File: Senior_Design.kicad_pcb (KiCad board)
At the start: 2 copper layers, 100 x 100 mm, 149 parts, among them J101 BARREL_JACK, J102 touch(8pos) AT42QT1070 STANDA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, J103 ISP, J104 GS3, J105 GS3, J106 GS3, J107 LoadCell_Conn, J108 Smraza2004_LCD, J109 ambientLight, J110 GS3, J1101 BLE_RESET, J111 RESET, J112 Serial Monitor, J113 breakout, J114 GS2, J115 GS2, J301 GS2, J501 USB_A, J502 USB_A, Q1101 BSS138, Q1102 BSS138, Q301 MMBT4403, U1001 INA169, U102 WS2812B, U103 WS2812B_STRIP, U104 ATMEGA328PB-AU, U1101 LM358_IC, U1102 LP2985-3.3, U201 TPS562210, U301 HX711, U401 MOUDLE-BLUETOOTH-HC-05(34P-27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, U601 TPS562210, U901 INA169, Y101 16MHZ

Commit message: traces started
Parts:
- removed C101: 0.1uF, Capacitors_SMD:C_0603
- removed D202, D602: LED, LEDs:LED_0805
- removed J114, J115: GS2, Connectors:GS2
- removed R206, R606: 1K, Resistors_SMD:R_0603
- removed R401: 10K, Resistors_SMD:R_0603
- removed S401: button, Buttons_Switches_THT:SW_PUSH_6mm
- added C104: 0.1uF, Capacitors_SMD:C_0603, F.Cu at (105.0, 122.0)
- added D105: LED, LEDs:LED_0603, F.Cu at (111.0, 102.0)
- added D106: LED, LEDs:LED_0603, F.Cu at (111.0, 105.0)
- added D1105: LED, LEDs:LED_0603, F.Cu at (76.0, 67.0)
- added J1102: GS2, Connectors:GS2, F.Cu at (60.4, 110.0)
- added J1103: GS2, Connectors:GS2, F.Cu at (54.0, 110.0)
- added J117: GS3, Connectors:GS3, F.Cu at (126.0, 106.0)
- added J118: GS3, Connectors:GS3, F.Cu at (119.0, 106.0)
- added J119: ext_5VPWR, Pin_Headers:Pin_Header_Straight_1x04_Pitch2.54mm, F.Cu at (107.0, 113.0)
- added J123: GS2, Connectors:GS2, F.Cu at (91.2, 76.6)
- added J124: ext_Motion, Pin_Headers:Pin_Header_Straight_1x03_Pitch2.54mm, F.Cu at (101.0, 122.0)
- added J302: GS2, Connectors:GS2, F.Cu at (66.0, 118.0)
- added J401: GS2, Connectors:GS2, F.Cu at (137.0, 107.0)
- added J402: GS2, Connectors:GS2, F.Cu at (137.0, 128.0)
- added R109: 500, Resistors_SMD:R_0805_HandSoldering, F.Cu at (107.0, 102.0)
- added R110: 500, Resistors_SMD:R_0805_HandSoldering, F.Cu at (107.0, 105.0)
- added R1112: 500, Resistors_SMD:R_0805_HandSoldering, F.Cu at (71.0, 67.0)
- added R1113: 500, Resistors_SMD:R_0805_HandSoldering, F.Cu at (55.0, 64.0)
- added R801: 10, Resistors_THT:R_Axial_DIN0309_L9.0mm_D3.2mm_P5.08mm_Vertical, F.Cu at (122.0, 89.0)
- added R802: RL, Resistors_THT:R_Axial_DIN0309_L9.0mm_D3.2mm_P5.08mm_Vertical, F.Cu at (132.0, 85.0)
- added R902: 10, Resistors_THT:R_Axial_DIN0309_L9.0mm_D3.2mm_P5.08mm_Vertical, F.Cu at (137.0, 89.0)
- added R903: RL, Resistors_THT:R_Axial_DIN0309_L9.0mm_D3.2mm_P5.08mm_Vertical, F.Cu at (117.0, 85.0)
- C112, C113: value 22pF -> 20pF
- C204, C604: footprint Capacitors_SMD:C_0603 -> Capacitors_SMD:C_0402
- D101, D102, D103, D104, D1103, D401: footprint LEDs:LED_0805 -> LEDs:LED_0603
- D1104, D201, D501, D502, D601: footprint Diodes_SMD:D_SOD-123F -> sod:SOD-128
- L201, L601: footprint Inductors_SMD:L_Vishay_IHLP-1212 -> Inductors_SMD:L_Taiyo-Yuden_MD-5050
- R101, R107, R108, R301, R302: footprint Resistors_SMD:R_0603 -> Resistors_SMD:R_0805_HandSoldering
- R102: value 1K -> 500; footprint Resistors_SMD:R_0603 -> Resistors_SMD:R_0805_HandSoldering
- R103, R1102, R1104: value 330 -> 500; footprint Resistors_SMD:R_0603 -> Resistors_SMD:R_0805_HandSoldering
- R1101: value 1k -> 10k
- R1103: value 33K -> 54.9K
- R1105: value 220 -> 100; footprint Resistors_SMD:R_0603 -> Resistors_SMD:R_0805_HandSoldering
- R201, R601: value 10.0k -> 10k
- R203, R603: value 54.9k -> 59k
- R204, R604: value 10k -> 10k_FB
- R205, R605: value 0.1 -> 0.1_SHUNT; footprint Resistors_SMD:R_0603 -> Resistors_SMD:R_1206
- R406: value 2K -> 500; footprint Resistors_SMD:R_0603 -> Resistors_SMD:R_0805_HandSoldering
- RV1101: footprint Potentiometers:Potentiometer_Trimmer_ACP_CA9v_Horizontal_Px10.0mm_Py5.0mm -> SparkFun-Electromechanical:TSR-3386U
- U1001, U901: footprint sot:SOT23-5 -> TO_SOT_Packages_SMD:SOT-23-5
- U201, U601: value TPS562210 -> TPS563210ADDFT
- U301: footprint sop:SSOP16 -> soic:SOIC16
- moved D1103 22.5 mm to (113.0, 125.0), turned to 0 degrees
- moved R1104 21.6 mm to (113.0, 122.0), turned to 0 degrees
- moved C111 19.4 mm to (92.0, 82.0), turned to 180 degrees
- moved C110 19.1 mm to (92.0, 80.0), turned to 180 degrees
- moved D401 13.6 mm to (76.0, 70.0)
- moved R406 12.6 mm to (71.0, 70.0)
- moved D103 12.5 mm to (104.0, 68.0), turned to 180 degrees
- moved R405 12.5 mm to (64.0, 68.0), turned to 90 degrees
- moved R1101 9.22 mm to (105.0, 125.0), turned to 180 degrees
- moved R107 8.54 mm to (105.0, 65.0), turned to 180 degrees
- moved J102 8.25 mm to (90.0, 113.0)
- moved C303 7.62 mm to (67.0, 129.0), turned to 180 degrees
- moved J109 6.71 mm to (111.0, 76.0)
- moved D501 6.40 mm to (133.0, 107.0)
- moved D502 6.40 mm to (133.0, 128.0)
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- renumbered S101 to SW101, J111 to SW102, J1101 to SW1101
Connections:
- net BT_PWR renamed /Bluetooth/PwrOn
- C106 pad 2: 5V-BUS -> 5V-BUS_USBLINE
- C107 pad 2: 5V-BUS -> 5V-BUS_USBLINE
- C108 pad 2: 5V-BUS -> 5V-BUS_USBLINE
- C110 pad 2: 5V-BUS -> Net-(C110-Pad2)
- C111 pad 2: 5V-BUS -> Net-(C110-Pad2)
- C305 pad 2: 3V3-BUS -> 5V-BUS
- C306 pad 1: 3V3-BUS -> 5V-BUS
- D1104 pad 2: 3V3-BUS -> 5V-BUS
- D201 pad 1: 5V-BUS -> /_5V_SYS
- D501 pad 2: /USB/5V -> 5V-BUS_USBLINE
- D502 pad 2: /USB/5V -> 5V-BUS_USBLINE
- D601 pad 1: 5V-BUS_USBLINE -> /_5V_USB
- J103 pad 2: (no net) -> 5V-BUS
- Q301 pad 3: 3V3-BUS -> 5V-BUS
- R103 pad 1: (no net) -> LED_Din
- R107 pad 2: Net-(J114-Pad1) -> MCU_TX
- R108 pad 2: Net-(J115-Pad1) -> MCU_RX
- R1101 pad 2: (no net) -> Motion_Signal
- R1110 pad 2: 3V3-BUS -> 5V-BUS
- R1111 pad 2: 3V3-BUS -> 5V-BUS
- R305 pad 1: 3V3-BUS -> 5V-BUS
- U102 pad 1: 5V-BUS -> 5V-BUS_USBLINE
- U103 pad 3: 5V-BUS -> 5V-BUS_USBLINE
- U104 pad 18: 5V-BUS -> Net-(C110-Pad2)
- U104 pad 2: (no net) -> BT_KEY
- U104 pad 20: 5V-BUS -> Net-(C110-Pad2)
- U104 pad 23: (no net) -> Motion_Signal
- U104 pad 4: 5V-BUS -> Net-(C110-Pad2)
- U104 pad 9: LEDS_Din -> LED_Din
- U301 pad 1: 3V3-BUS -> 5V-BUS
- U301 pad 16: 3V3-BUS -> 5V-BUS
- U401 pad 1: B_RX -> /Bluetooth/TX_3v3
- U401 pad 11: Net-(R401-Pad2) -> (no net)
- U401 pad 2: B_TX -> /Bluetooth/RX_3v3
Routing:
- net 5V-BUS: track 0.00 -> 186.8 mm, vias 0 -> 6
- net 5V-BUS_USBLINE: track 0.00 -> 70.6 mm, vias 0 -> 2
- net +12V: track 99.3 -> 144.1 mm
- net /Bluetooth/3_3V: track 0.00 -> 31.9 mm, vias 0 -> 4
- net /5V-Regulator/PG: track 16.8 -> 48.3 mm, vias 2 -> 4
- net Net-(RV1101-Pad2): track 0.00 -> 31.3 mm
- net 5V_curMon+_USBLINE: track 0.00 -> 29.5 mm, vias 0 -> 2
- net Net-(D1102-Pad2): track 0.00 -> 25.8 mm
- net /Bluetooth/RX_3v3: track 2.15 -> 26.6 mm
- net /Bluetooth/TX_3v3: track 2.15 -> 25.5 mm
- net 5V_curMon+: track 15.1 -> 37.0 mm, vias 0 -> 2
- net Net-(R401-Pad2): track 20.0 -> 0.00 mm
- net /_5V_USB: track 0.00 -> 18.3 mm
- net Net-(J117-Pad3): track 0.00 -> 17.0 mm
- net Net-(C110-Pad2): track 0.00 -> 15.5 mm
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
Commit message: 99 percent ready to order
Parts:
- removed R801, R902: 10, Resistors_THT:R_Axial_DIN0309_L9.0mm_D3.2mm_P5.08mm_Vertical
- moved R704 26.0 mm to (127.2, 114.0), turned to 270 degrees
- moved R703 22.0 mm to (127.2, 111.0), turned to 270 degrees
- moved R702 21.7 mm to (121.0, 114.8), turned to 270 degrees
- moved R903 18.0 mm to (134.9, 84.0)
- moved R701 16.6 mm to (121.0, 112.0), turned to 270 degrees
- moved R802 15.5 mm to (116.5, 84.0)
- moved R901 15.2 mm to (119.8, 94.0)
- moved U901 15.2 mm to (120.8, 98.0)
- moved R1001 14.9 mm to (134.9, 94.0)
- moved U1001 14.8 mm to (135.8, 98.0)
- moved C104 6.75 mm to (98.3, 122.8), turned to 90 degrees
- moved C107 5.10 mm to (110.0, 53.0), turned to 90 degrees
- moved J106 4.08 mm to (108.8, 92.0)
- moved R102 3.43 mm to (138.4, 58.2)
- moved D101 3.37 mm to (134.4, 58.2)
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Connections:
- J501 pad 5: Net-(J501-Pad5) -> GND
- J502 pad 5: Net-(J502-Pad5) -> GND
- R202 pad 1: /5V-Regulator/PG -> 5V_curMon+
- R202 pad 2: 5V_curMon+ -> Net-(R202-Pad2)
- R602 pad 1: /5V-Regulator/PG -> 5V_curMon+_USBLINE
- R602 pad 2: 5V_curMon+_USBLINE -> Net-(R602-Pad2)
- U201 pad 4: /5V-Regulator/PG -> Net-(R202-Pad2)
- U601 pad 4: /5V-Regulator/PG -> Net-(R602-Pad2)
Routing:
- net 5V-BUS: track 186.8 -> 432.6 mm, vias 6 -> 13
- net GND: track 14.5 -> 183.0 mm, vias 7 -> 37
- net SDA: track 3.28 -> 90.4 mm, vias 0 -> 1
- net SCL: track 3.41 -> 88.4 mm, vias 0 -> 1
- net 5V-BUS_USBLINE: track 70.6 -> 148.4 mm, vias 2 -> 6
- net breakout_1A: track 0.00 -> 77.3 mm, vias 0 -> 1
- net BT_STATE: track 0.00 -> 70.6 mm, vias 0 -> 2
- net /Bluetooth/3_3V: track 31.9 -> 101.8 mm, vias 4 -> 6
- net LED_Din: track 0.00 -> 64.2 mm, vias 0 -> 2
- net MOSI: track 0.00 -> 63.2 mm, vias 0 -> 1
- net RESET: track 13.0 -> 75.5 mm, vias 0 -> 2
- net B_RX: track 11.8 -> 74.3 mm, vias 0 -> 1
- net breakout_2A: track 0.00 -> 62.4 mm, vias 0 -> 1
- net SCK: track 3.14 -> 61.8 mm, vias 0 -> 2
- net MISO: track 0.00 -> 57.6 mm, vias 0 -> 1
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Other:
- board text added: "5V D GND"
- board text added: "5V GND 5V_USB GND"
- board text added: "5V SIG GND"
- board text added: "Bluetooth"
- board text added: "Bluetooth RESET"
- board text added: "E+ E- A- A+"
- board text added: "EXTERNAL 5V POWER"
- board text added: "GND 5V SDA SCL"
- board text added: "GND LED 5V"
- board text added: "MCU RESET"
- board text added: "MISO-VCC SCK-MOSS RES-GND"
- board text added: "Monitor"
- board text added: "PC3 PE2 5V GND"
- board text added: "PE0 PE1 PB0 PB1"
- board text added: "RX TX"
- board text added: "UART"
- board text added: "UCF Senior Design Smart Table"

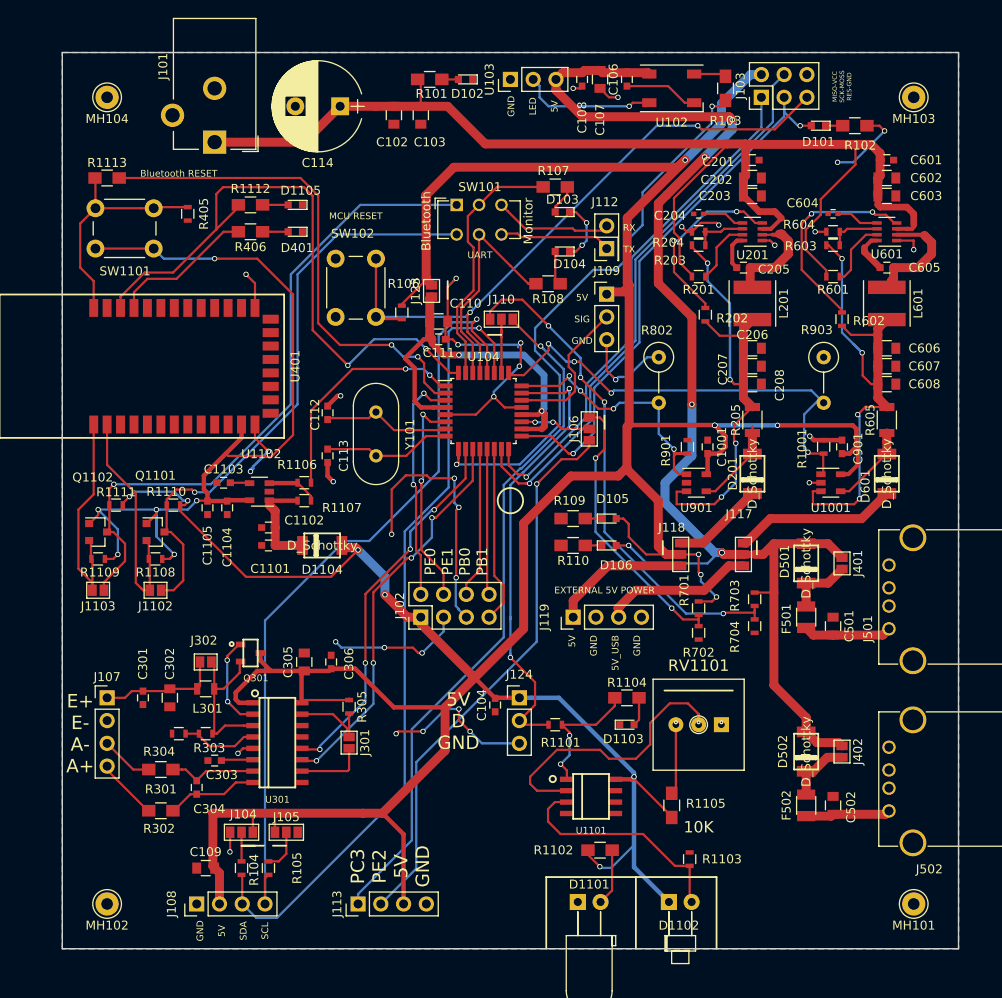
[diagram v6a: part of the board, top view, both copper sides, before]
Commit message: finalized pcblayouts, before uploading to manufacturer
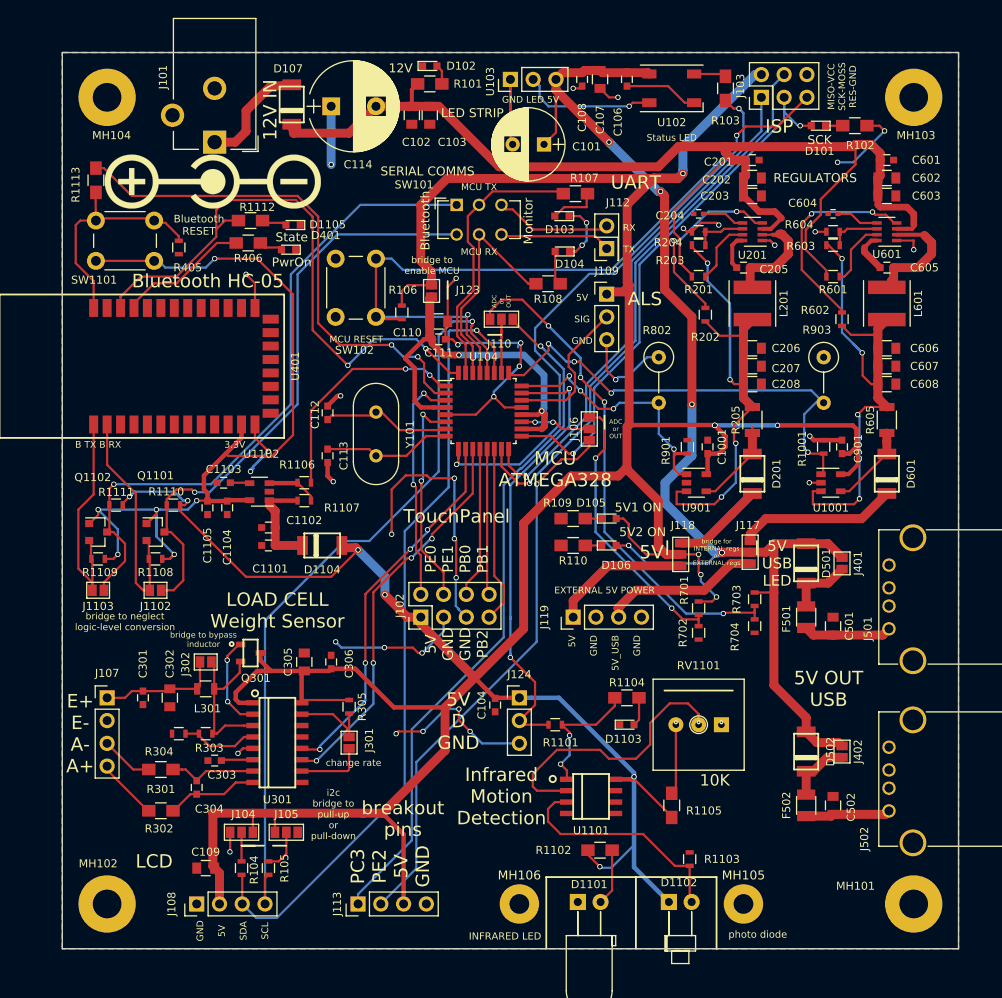
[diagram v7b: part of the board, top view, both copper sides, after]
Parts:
- added C101: ?uF, Capacitors_THT:CP_Radial_D8.0mm_P3.50mm, F.Cu at (103.8, 60.2)
- added D107: D_Schottky, seniorDesign:SOD-128, F.Cu at (75.6, 55.8)
- added MH105: IR LIGHT BLOCKER MOUNT, Mounting_Holes:MountingHole_2.2mm_M2_Pad, F.Cu at (126.0, 145.0)
- added MH106: IR LIGHT BLOCKER MOUNT, Mounting_Holes:MountingHole_2.2mm_M2_Pad, F.Cu at (101.0, 145.0)
- added REF***: Polarity_Center_Positive_6mm_SilkScreen, Symbols:Polarity_Center_Positive_6mm_SilkScreen, F.Cu at (66.8, 64.4)
- D1104, D201, D501, D502, D601: footprint sod:SOD-128 -> seniorDesign:SOD-128
- MH101, MH102, MH103, MH104: footprint Connectors:Pin_d1.3mm_L11.0mm -> Mounting_Holes:MountingHole_3.2mm_M3_Pad
- moved D102 4.27 mm to (91.0, 51.5), turned to 0 degrees
- moved R405 3.88 mm to (63.0, 71.8)
- moved R107 2.37 mm to (107.2, 65.8)
- moved D1105 2.26 mm to (75.8, 69.2)
- moved D401 2.14 mm to (75.2, 72.0)
- moved C102 2.00 mm to (89.0, 57.0)
- moved R1112 1.75 mm to (71.0, 68.8)
- moved SW1101 1.38 mm to (53.8, 68.8)
- moved R1113 1.27 mm to (53.8, 64.2), turned to 90 degrees
- moved R406 1.27 mm to (70.8, 71.2)
- moved C103 1.00 mm to (91.0, 57.0)
- moved C114 1.00 mm to (80.0, 56.0), turned to 0 degrees
- moved J117 0.79 mm to (126.8, 105.8)
- moved R101 0.50 mm to (91.0, 53.5)
- moved D103 0.45 mm to (105.8, 68.2)
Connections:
- C114 pad 1: +12V -> GND
- C114 pad 2: GND -> +12V
- J101 pad 1: +12V -> Net-(D107-Pad2)
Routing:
- net GND: track 183.0 -> 200.4 mm, vias 37 -> 38
- net Net-(D107-Pad2): track 0.00 -> 12.5 mm
- net RESET: track 75.5 -> 84.6 mm
- net +12V: track 144.8 -> 139.8 mm
- net BT_STATE: track 70.6 -> 66.0 mm
- net 5V-BUS_USBLINE: track 148.4 -> 144.3 mm
- net MCU_TX: track 28.7 -> 30.8 mm
- net Net-(D103-Pad2): track 3.36 -> 5.32 mm
- net BT_KEY: track 55.9 -> 57.6 mm
- net LED_Din: track 64.2 -> 65.8 mm
- net /Bluetooth/PwrOn: track 16.2 -> 14.7 mm
- net SCL: track 88.4 -> 87.4 mm
- net Net-(J117-Pad3): track 17.0 -> 17.8 mm
- net SDA: track 90.4 -> 89.9 mm
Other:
- board text added: "12V"
- board text added: "12V IN"
- board text added: "3.3V"
- board text added: "5V"
- board text added: "5V GND GND PB2"
- board text added: "5V OUT USB"
- board text added: "5V USB LED"
- board text added: "5V1 ON"
- board text added: "5V2 ON"
- board text added: "ADC or OUT"
- board text added: "ALS"
- board text added: "B TX B RX"
- board text added: "Bluetooth HC-05"
- board text added: "INFRARED LED"
- board text added: "ISP"
- board text added: "Infrared Motion Detection"
- board text added: "LCD"
- board text added: "LED STRIP"
- board text added: "LOAD CELL Weight Sensor"
- board text added: "MCU ATMEGA328"
- board text added: "MCU RX"
- board text added: "MCU TX"
- board text added: "PCB designed by Theodore Cox --------------------------------- Software developed by Christopher Corley Dhaval Desai Mikey Garrity ---------------------------------"
- board text added: "PwrOn"
- board text added: "REGULATORS"
- board text added: "SCK"
- board text added: "SERIAL COMMS"
- board text added: "State"
- board text added: "Status LED"
- board text added: "TouchPanel"
- board text added: "UCF Senior Design Smart Table Summer 2018"
- board text added: "breakout pins"
- board text added: "bridge for INTERNAL regs or EXTERNAL regs"
- board text added: "bridge to bypass inductor"
- board text added: "bridge to enable MCU"
- board text added: "bridge to neglect logic-level conversion"
- board text added: "change rate"
- board text added: "i2c bridge to pull-up or pull-down"
- board text added: "photo diode"
- board text removed: "UCF Senior Design Smart Table"

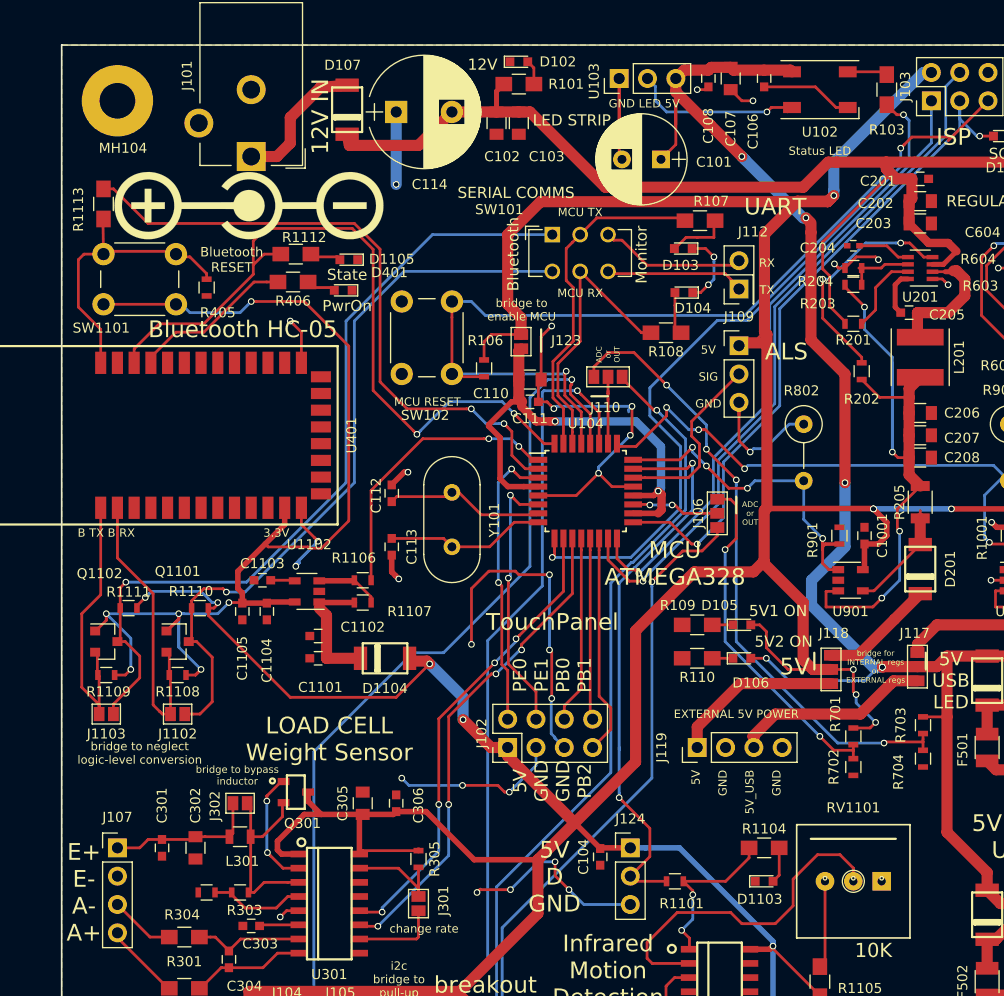
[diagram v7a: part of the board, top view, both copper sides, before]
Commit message: new touch implementation
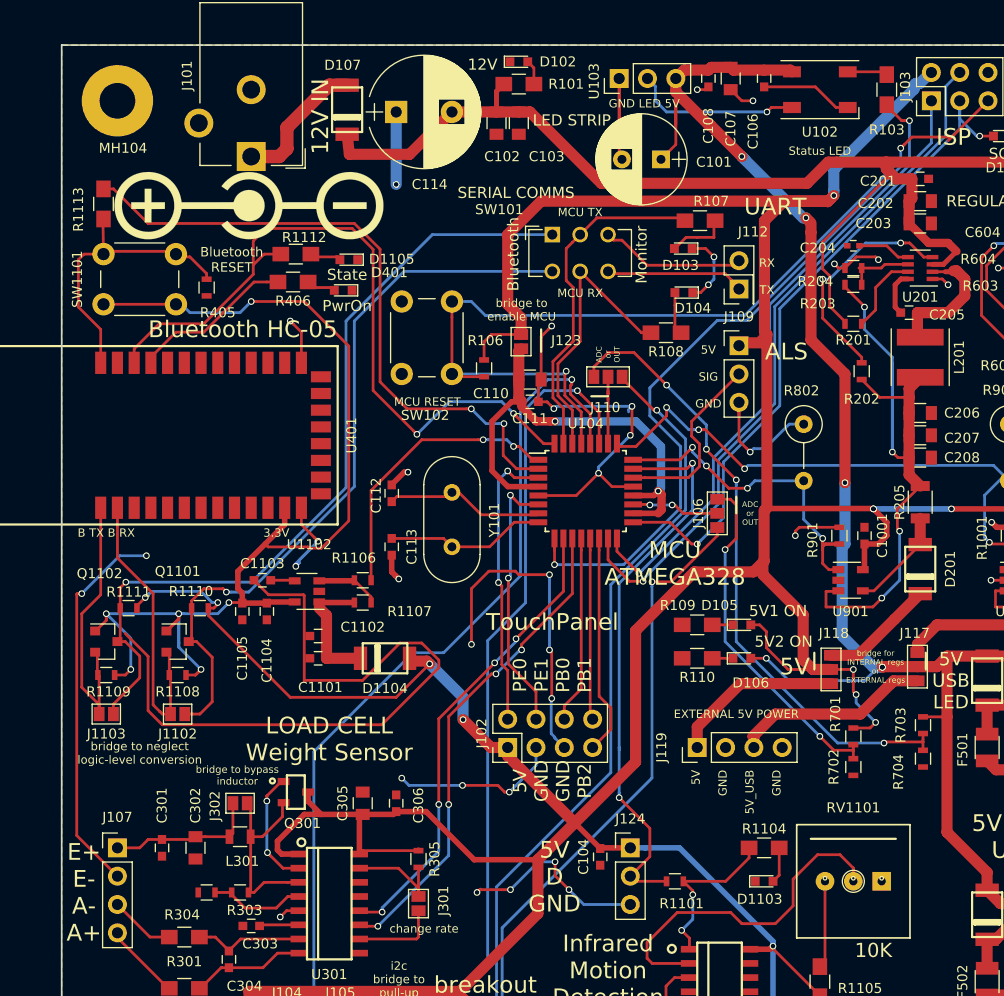
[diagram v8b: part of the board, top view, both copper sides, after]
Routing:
- net GND: track 200.4 -> 303.4 mm, vias 38 -> 41
- net 5V-BUS_USBLINE: track 144.3 -> 142.0 mm
- net +12V: track 139.8 -> 140.7 mm
- net LED_Din: track 65.8 -> 66.5 mm
- net 5V_curMon-: track 9.72 -> 9.02 mm
- net BT_KEY: track 57.6 -> 58.1 mm
- net 5V-BUS: track 432.4 -> 432.9 mm
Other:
- board text added: "--------------------------------- PCB designed by Theodore Cox Software developed by Christopher Corley Dhaval Desai Mikey Garrity ---------------------------------"
- board text removed: "PCB designed by Theodore Cox --------------------------------- Software developed by Christopher Corley Dhaval Desai Mikey Garrity ---------------------------------"
